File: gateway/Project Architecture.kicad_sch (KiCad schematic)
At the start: 0 parts

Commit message: Working on first version
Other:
- sheet Interfaces renamed LoRa
- sheet Radio renamed Zigbee
- added sheet Ethernet (Ethernet.kicad_sch)
- added sheet Peripherals (Peripherals.kicad_sch)
- added sheet wMBus (WmBus.kicad_sch)
- sheet LoRa: file Interfaces.kicad_sch -> LoRa.kicad_sch
- sheet Power: file Power A.kicad_sch -> Power.kicad_sch
- sheet Zigbee: file Radio.kicad_sch -> Zigbee.kicad_sch
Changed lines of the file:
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@@
 			(color 255 200 0 0.502)
 		)
-		(property "Sheetname" "Interfaces"
+		(property "Sheetname" "LoRa"
 			(at 251.46 75.1709 0)
 			(show_name no)
@@
 			)
 		)
-		(property "Sheetfile" "Interfaces.kicad_sch"
+		(property "Sheetfile" "LoRa.kicad_sch"
 			(at 251.46 97.1046 0)
 			(show_name no)
@@
 			(color 255 200 0 0.502)
 		)
-		(property "Sheetname" "Radio"
+		(property "Sheetname" "Zigbee"
 			(at 298.45 75.1709 0)
 			(show_name no)
@@
 			)
 		)
-		(property "Sheetfile" "Radio.kicad_sch"
+		(property "Sheetfile" "Zigbee.kicad_sch"
 			(at 298.45 97.1046 0)
 			(show_name no)
@@
 				(path "/d5742f03-3b1a-42e5-a384-018bd4b919aa/c5103ceb-5325-4a84-a025-9638a412984e"
 					(page "10")
+				)
+			)
+		)
+	)
+	(sheet
+		(at 224.79 146.05)
+		(size 36.83 20.32)
+		(exclude_from_sim no)
+		(in_bom yes)
+		(on_board yes)
+		(dnp no)
+		(fields_autoplaced yes)
+		(stroke
+			(width 0.1524)
+			(type solid)
+		)
+		(fill
+			(color 255 200 0 0.502)
+		)
+		(property "Sheetname" "wMBus"
+			(at 224.79 145.0209 0)
+			(show_name no)
+			(do_not_autoplace no)
+			(effects
+				(font
+					(size 1.905 1.905)
+					(bold yes)
+				)
+				(justify left bottom)
+			)
+		)
+		(property "Sheetfile" "WmBus.kicad_sch"
+			(at 224.79 166.9546 0)
+			(show_name no)
+			(do_not_autoplace no)
+			(effects
+				(font
+					(face "Arial")
+					(size 1.27 1.27)
+				)
+				(justify left top)
+			)
+		)
+		(instances
+			(project "Gateway"
+				(path "/d5742f03-3b1a-42e5-a384-018bd4b919aa/c5103ceb-5325-4a84-a025-9638a412984e"
+					(page "12")
+				)
+			)
+		)
+	)
+	(sheet
+		(at 271.78 144.78)
+		(size 36.83 20.32)
+		(exclude_from_sim no)
+		(in_bom yes)
+		(on_board yes)
+		(dnp no)
+		(fields_autoplaced yes)
+		(stroke
+			(width 0.1524)
+			(type solid)
+		)
+		(fill
+			(color 255 200 0 0.502)
+		)
+		(property "Sheetname" "Peripherals"
+			(at 271.78 143.7509 0)
+			(show_name no)
+			(do_not_autoplace no)
+			(effects
+				(font
+					(size 1.905 1.905)
+					(bold yes)
+				)
+				(justify left bottom)
+			)
+		)
+		(property "Sheetfile" "Peripherals.kicad_sch"
+			(at 271.78 165.6846 0)
+			(show_name no)
+			(do_not_autoplace no)
+			(effects
+				(font
+					(face "Arial")
+					(size 1.27 1.27)
+				)
+				(justify left top)
+			)
+		)
+		(instances
+			(project "Gateway"
+				(path "/d5742f03-3b1a-42e5-a384-018bd4b919aa/c5103ceb-5325-4a84-a025-9638a412984e"
+					(page "11")
+				)
+			)
+		)
+	)
+	(sheet
+		(at 271.78 180.34)
+		(size 36.83 20.32)
+		(exclude_from_sim no)
+		(in_bom yes)
+		(on_board yes)
+		(dnp no)
+		(fields_autoplaced yes)
+		(stroke
+			(width 0.1524)
+			(type solid)
+		)
+		(fill
+			(color 255 200 0 0.502)
+		)
+		(property "Sheetname" "Ethernet"
+			(at 271.78 179.3109 0)
+			(show_name no)
+			(do_not_autoplace no)
+			(effects
+				(font
+					(size 1.905 1.905)
+					(bold yes)
+				)
+				(justify left bottom)
+			)
+		)
+		(property "Sheetfile" "Ethernet.kicad_sch"
+			(at 271.78 201.2446 0)
+			(show_name no)
+			(do_not_autoplace no)
+			(effects
+				(font
+					(face "Arial")
+					(size 1.27 1.27)
+				)
+				(justify left top)
+			)
+		)
+		(instances
+			(project "Gateway"
+				(path "/d5742f03-3b1a-42e5-a384-018bd4b919aa/c5103ceb-5325-4a84-a025-9638a412984e"
+					(page "13")
 				)
 			)
@@
 			)
 		)
-		(property "Sheetfile" "Power A.kicad_sch"
+		(property "Sheetfile" "Power.kicad_sch"
 			(at 190.5 97.1046 0)
 			(show_name no)

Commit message: Working on version 1.0
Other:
- added sheet NVMe (NVMe.kicad_sch)
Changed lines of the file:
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@@
+	)
+	(sheet
+		(at 168.91 147.32)
+		(size 36.83 20.32)
+		(exclude_from_sim no)
+		(in_bom yes)
+		(on_board yes)
+		(dnp no)
+		(fields_autoplaced yes)
+		(stroke
+			(width 0.1524)
+			(type solid)
+		)
+		(fill
+			(color 255 200 0 0.502)
+		)
+		(property "Sheetname" "NVMe"
+			(at 168.91 146.2909 0)
+			(show_name no)
+			(do_not_autoplace no)
+			(effects
+				(font
+					(size 1.905 1.905)
+					(bold yes)
+				)
+				(justify left bottom)
+			)
+		)
+		(property "Sheetfile" "NVMe.kicad_sch"
+			(at 168.91 168.2246 0)
+			(show_name no)
+			(do_not_autoplace no)
+			(effects
+				(font
+					(face "Arial")
+					(size 1.27 1.27)
+				)
+				(justify left top)
+			)
+		)
+		(instances
+			(project "Gateway"
+				(path "/d5742f03-3b1a-42e5-a384-018bd4b919aa/c5103ceb-5325-4a84-a025-9638a412984e"
+					(page "14")
+				)
+			)
+		)
 	)
 	(sheet

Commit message: Working on PCB
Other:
- sheet Battery ports: added I2C{I2C}, ~{Battery-Alert}, ~{Battery-Charge-Enable}, ~{Battery-Charge}; removed none
- sheet Ethernet ports: added Ethernet{Ethernet}; removed none
- sheet LoRa ports: added LoRa-Power-Enable, LoRa{LoRa}; removed none
- sheet NVMe ports: added PCIe{PCIe}, SSD-Power; removed none
- sheet Peripherals ports: added GPIO{GPIO}, I2C{I2C}, USB{D_P D_N ID VBUS}; removed none
- sheet Power ports: added PWR_1V8_MOCI, PowerMux-Status, SoM-Power-Enable; removed none
- sheet System on Module ports: added Ethernet{Ethernet}, GPIO{GPIO}, I2C{I2C}, LoRa-Power-Enable, LoRa{LoRa}, PCIe{PCIe}, PWR_1V8_MOCI, PowerMux-Status, SSD-Power, SoM-Power-Enable, USB{D_P D_N ID VBUS}, Zigbee-Power-Enable, Zigbee{Zigbee}, wM-Bus-Power-Enable, wM-Bus{wM-Bus}, ~{Battery-Alert}, ~{Battery-Charge-Enable}, ~{Battery-Charge}, ~{SoM-Peripheral-Reset}; removed none
- sheet Zigbee ports: added Zigbee-Power-Enable, Zigbee{Zigbee}; removed none
- sheet wMBus ports: added wM-Bus-Power-Enable, wM-Bus{wM-Bus}; removed none
- note added: "Page 10"
- note added: "Page 11"
- note added: "Page 12"
- note added: "Page 13"
- note added: "Page 9"

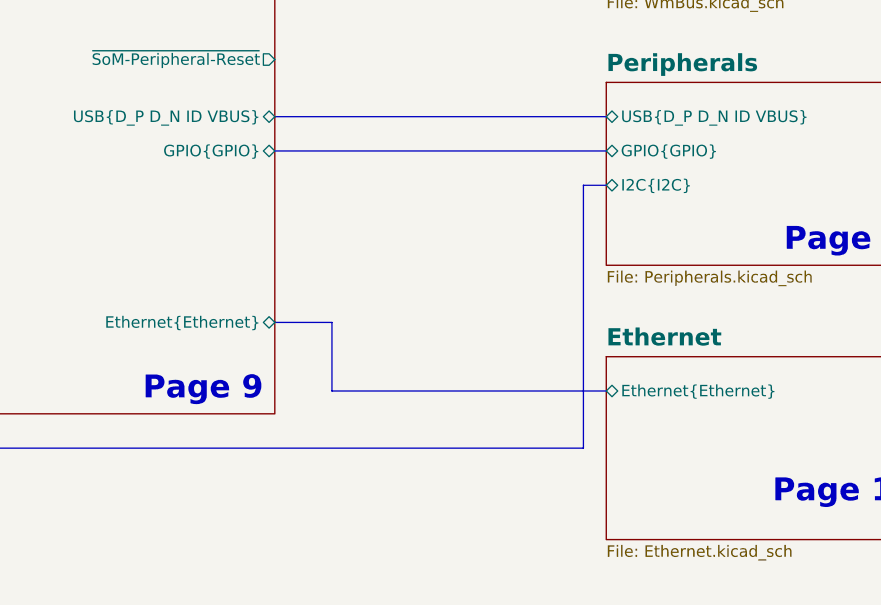
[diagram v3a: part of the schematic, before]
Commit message: Add WiFi antenna, add CAN interface
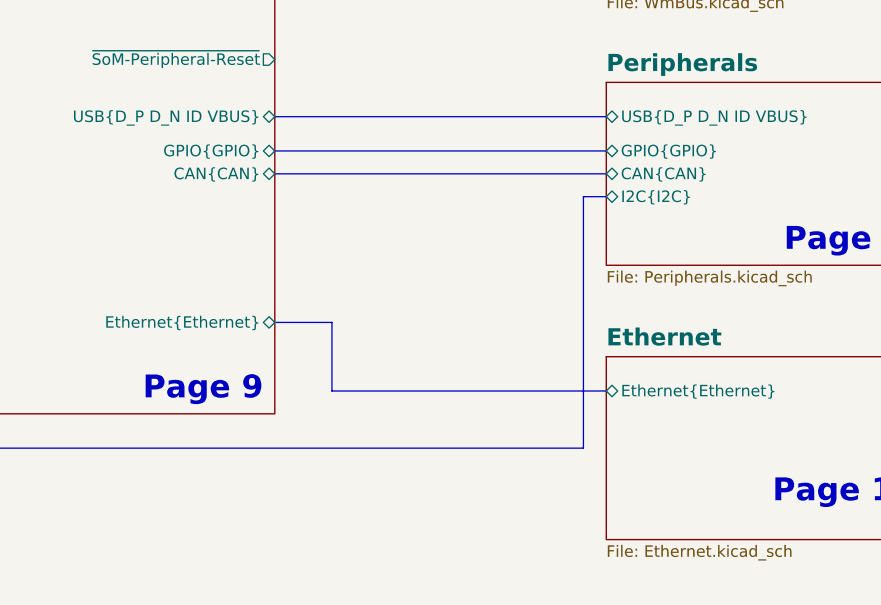
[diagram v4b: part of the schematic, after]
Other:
- sheet Peripherals ports: added CAN{CAN}; removed none
- sheet System on Module ports: added CAN{CAN}; removed none
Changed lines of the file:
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@@
+		)
+	)
+	(bus
+		(pts
+			(xy 226.06 142.24) (xy 262.89 142.24)
+		)
+		(stroke
+			(width 0)
+			(type default)
 		)
 	)
@@
 	(bus
 		(pts
-			(xy 260.35 143.51) (xy 262.89 143.51)
-		)
-		(stroke
-			(width 0)
-			(type default)
-		)
-	)
-	(bus
-		(pts
-			(xy 260.35 172.72) (xy 260.35 143.51)
+			(xy 260.35 144.78) (xy 262.89 144.78)
+		)
+		(stroke
+			(width 0)
+			(type default)
+		)
+	)
+	(bus
+		(pts
+			(xy 260.35 172.72) (xy 260.35 144.78)
 		)
 		(stroke
@@
 		)
 		(pin "I2C{I2C}" bidirectional
-			(at 262.89 143.51 180)
+			(at 262.89 144.78 180)
 			(effects
 				(font
@@
 		(pin "USB{D_P D_N ID VBUS}" bidirectional
 			(at 262.89 135.89 180)
+			(effects
+				(font
+					(size 1.27 1.27)
+				)
+				(justify left)
+			)
+		)
+		(pin "CAN{CAN}" bidirectional
+			(at 262.89 142.24 180)
 			(effects
 				(font
@@
 			)
 		)
+		(pin "CAN{CAN}" bidirectional
+			(at 226.06 142.24 0)
+			(effects
+				(font
+					(size 1.27 1.27)
+				)
+				(justify right)
+			)
+		)

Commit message: Working on version 1.0.0
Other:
- sheet NVMe ports: added ~{CTRL_WAKE1_MICO}; removed none
- sheet System on Module ports: added ~{CTRL_WAKE1_MICO}; removed none
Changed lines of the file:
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@@
+		)
+	)
+	(wire
+		(pts
+			(xy 163.83 165.1) (xy 176.53 165.1)
+		)
+		(stroke
+			(width 0)
+			(type default)
 		)
 	)
@@
 	(wire
 		(pts
+			(xy 148.59 173.99) (xy 163.83 173.99)
+		)
+		(stroke
+			(width 0)
+			(type default)
+		)
+	)
+	(wire
+		(pts
 			(xy 226.06 78.74) (xy 262.89 78.74)
 		)
@@
 		(pts
 			(xy 226.06 76.2) (xy 262.89 76.2)
+		)
+		(stroke
+			(width 0)
+			(type default)
+		)
+	)
+	(wire
+		(pts
+			(xy 163.83 173.99) (xy 163.83 165.1)
 		)
 		(stroke
@@
 			)
 		)
+		(pin "~{CTRL_WAKE1_MICO}" input
+			(at 148.59 173.99 0)
+			(effects
+				(font
+					(size 1.27 1.27)
+				)
+				(justify right)
+			)
+		)
 		(instances
 			(project "Gateway"
@@
 			)
 		)
+		(pin "~{CTRL_WAKE1_MICO}" output
+			(at 176.53 165.1 180)
+			(effects
+				(font
+					(size 1.27 1.27)
+				)
+				(justify left)
+			)
+		)

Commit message: Working on version 1.0.0
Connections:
- no-connect marks 0 -> 1
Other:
- added sheet Thread (Thread.kicad_sch)
- sheet System on Module ports: added Thread-Power-Enable, Thread{Thread}; removed none
- note added: "Page 15"

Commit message: Working on version 1.0.0
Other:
- sheet NVMe ports: added SSD-Power-Enable; removed SSD-Power
- sheet System on Module ports: added SSD-Power-Enable; removed SSD-Power
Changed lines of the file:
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@@
 			)
 		)
-		(pin "SSD-Power" input
+		(pin "SSD-Power-Enable" input
 			(at 148.59 181.61 0)
 			(effects
@@
 			)
 		)
-		(pin "SSD-Power" output
+		(pin "SSD-Power-Enable" output
 			(at 176.53 172.72 180)
 			(effects
